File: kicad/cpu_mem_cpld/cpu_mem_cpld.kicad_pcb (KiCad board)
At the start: 4 copper layers, 160 x 100.3 mm, 52 parts, among them J1 USB, P5 CONN_02X25, U1 W65C02S, U10 74HCT245, U11 16550, U13 MAX232, U2 CHUCK, U3 28C256, U4 512k x 8, U5 74LS06, U6 NE555, U9 74HCT245, X1 OSC, X2 OSC

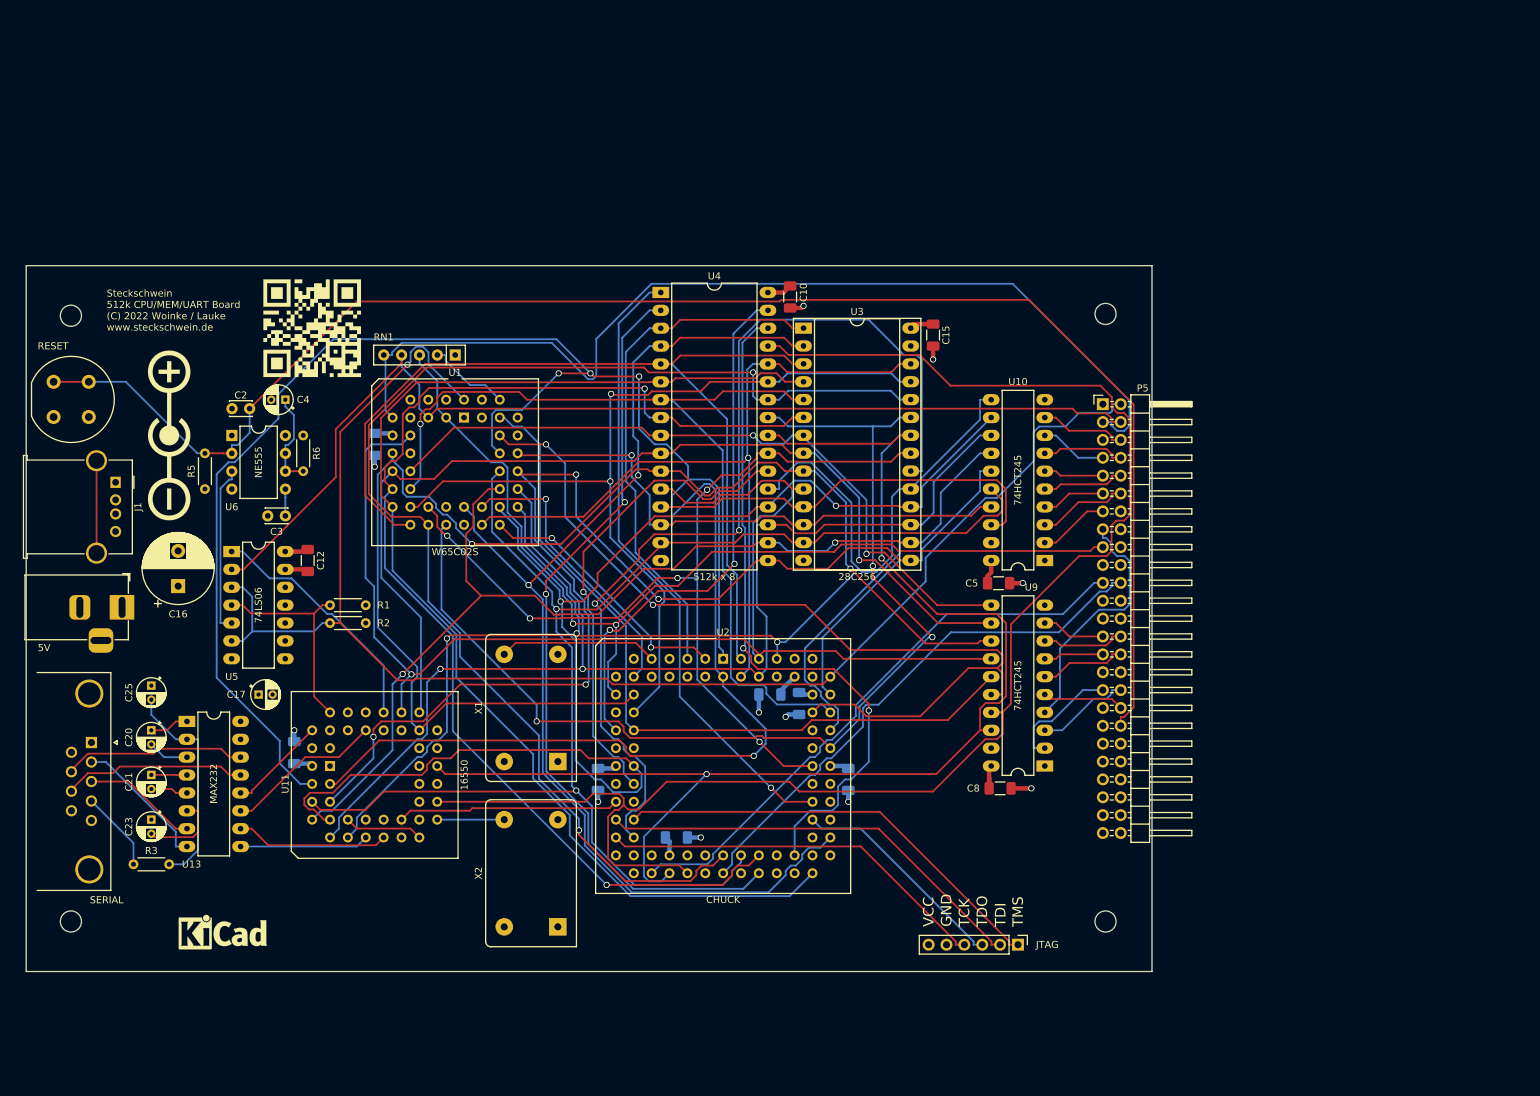
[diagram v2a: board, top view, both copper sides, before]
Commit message: added cs_uart2, /WE for EEPROM
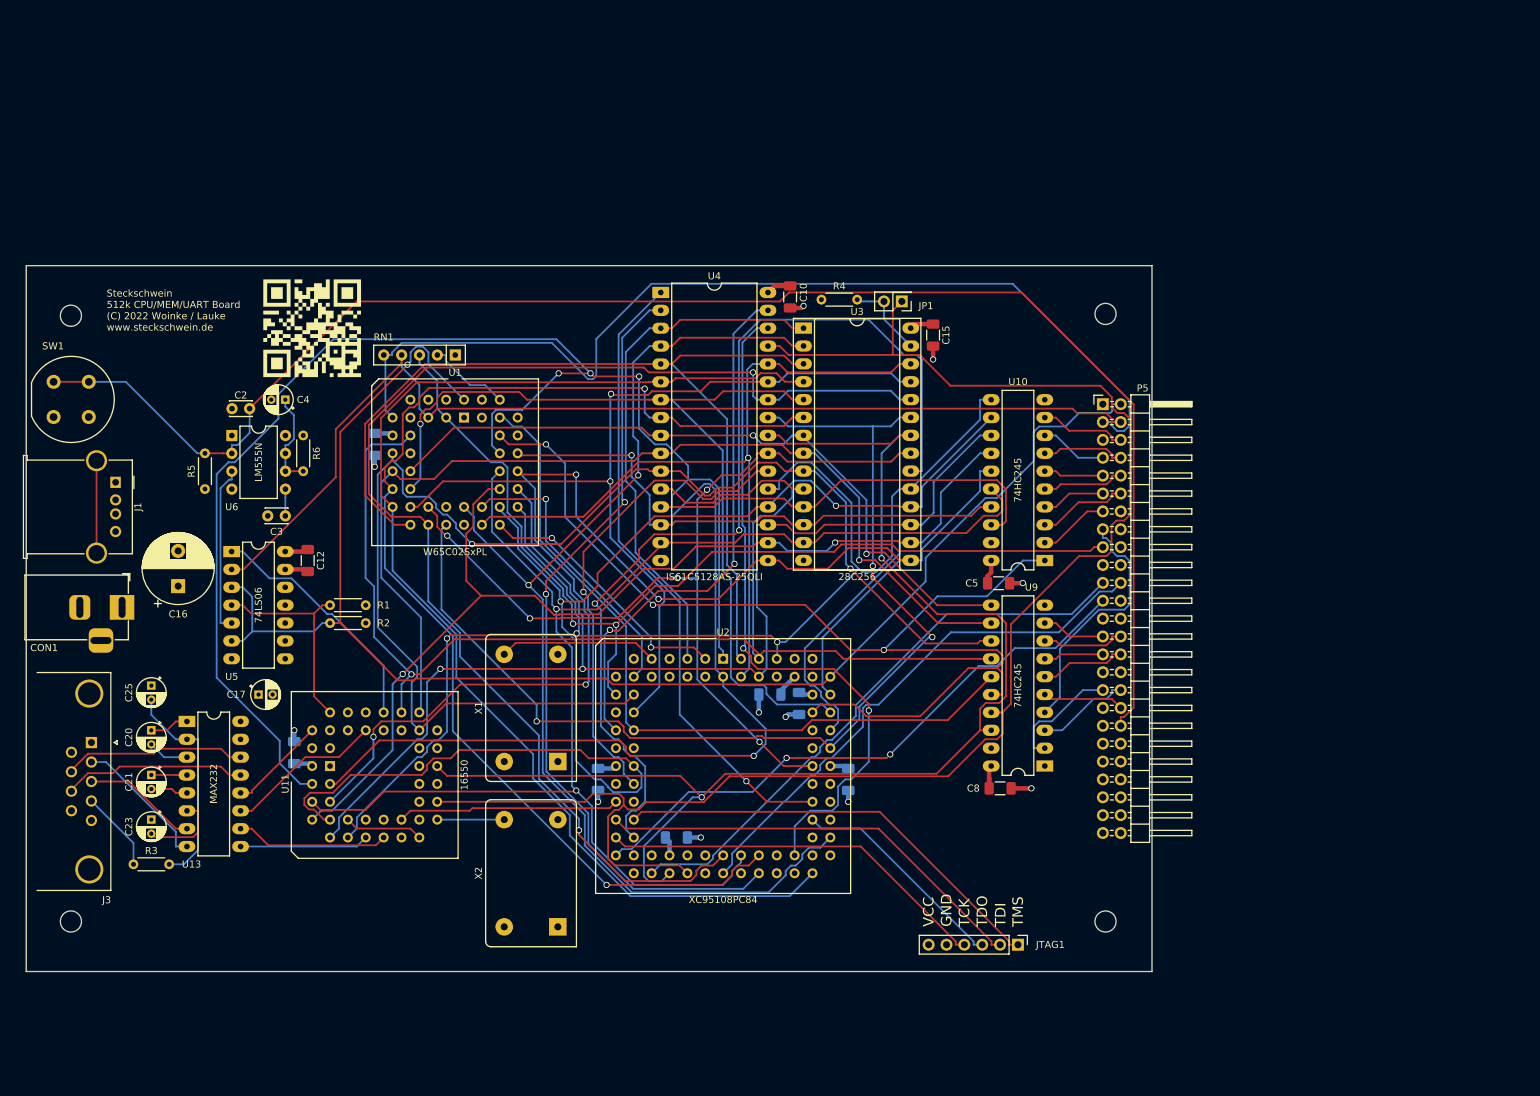
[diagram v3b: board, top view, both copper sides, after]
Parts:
- removed REF**: KiCad-Logo_5mm_SilkScreen, Symbol:KiCad-Logo_5mm_SilkScreen
- removed REF**: Polarity_Center_Positive_6mm_SilkScreen, Symbol:Polarity_Center_Positive_6mm_SilkScreen
- added JP1: Jumper_2_Open, Connector_PinHeader_2.54mm:PinHeader_2x01_P2.54mm_Vertical, F.Cu at (186.7, 50.8)
- added R4: 4k7, Resistor_THT:R_Axial_DIN0204_L3.6mm_D1.6mm_P5.08mm_Horizontal, F.Cu at (175.3, 50.5)
- U1: value W65C02S -> W65C02SxPL
- U10, U9: value 74HCT245 -> 74HC245
- U2: value CHUCK -> XC95108PC84
- U4: value 512k x 8 -> IS61C5128AS-25QLI
- U6: value NE555 -> LM555N
- renumbered 5V to CON1, SERIAL to J3, JTAG to JTAG1, RESET to SW1
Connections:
- U10 pad 1: /CPU_RW -> /CPU_R~{W}
- U2 pad 32: unconnected-(U2-Pad32) -> /~{CS_UART2}
- U3 pad 27: VCC -> Net-(U3-Pad27)
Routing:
- net /~{CS_UART2}: track 0.00 -> 84.2 mm, vias 0 -> 2
- net /CPU_R~{W}: track 126.9 -> 155.0 mm, vias 2 -> 3
- net Net-(U3-Pad27): track 0.00 -> 11.8 mm
- net /~{WE}: track 222.4 -> 229.4 mm
- net /RESET_TRIG: track 222.4 -> 223.2 mm
- net /EXT_A18: track 89.5 -> 90.1 mm

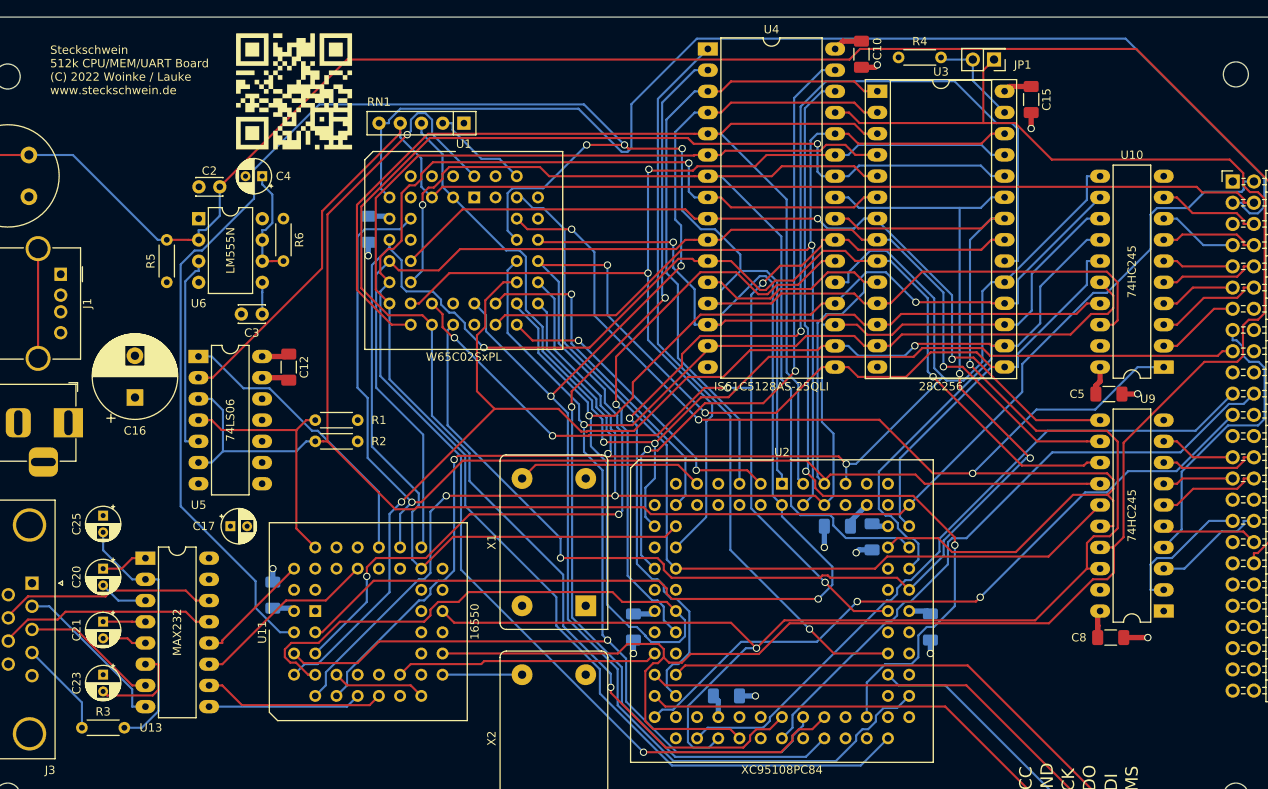
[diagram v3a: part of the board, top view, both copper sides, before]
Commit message: extra capacitor, revision text
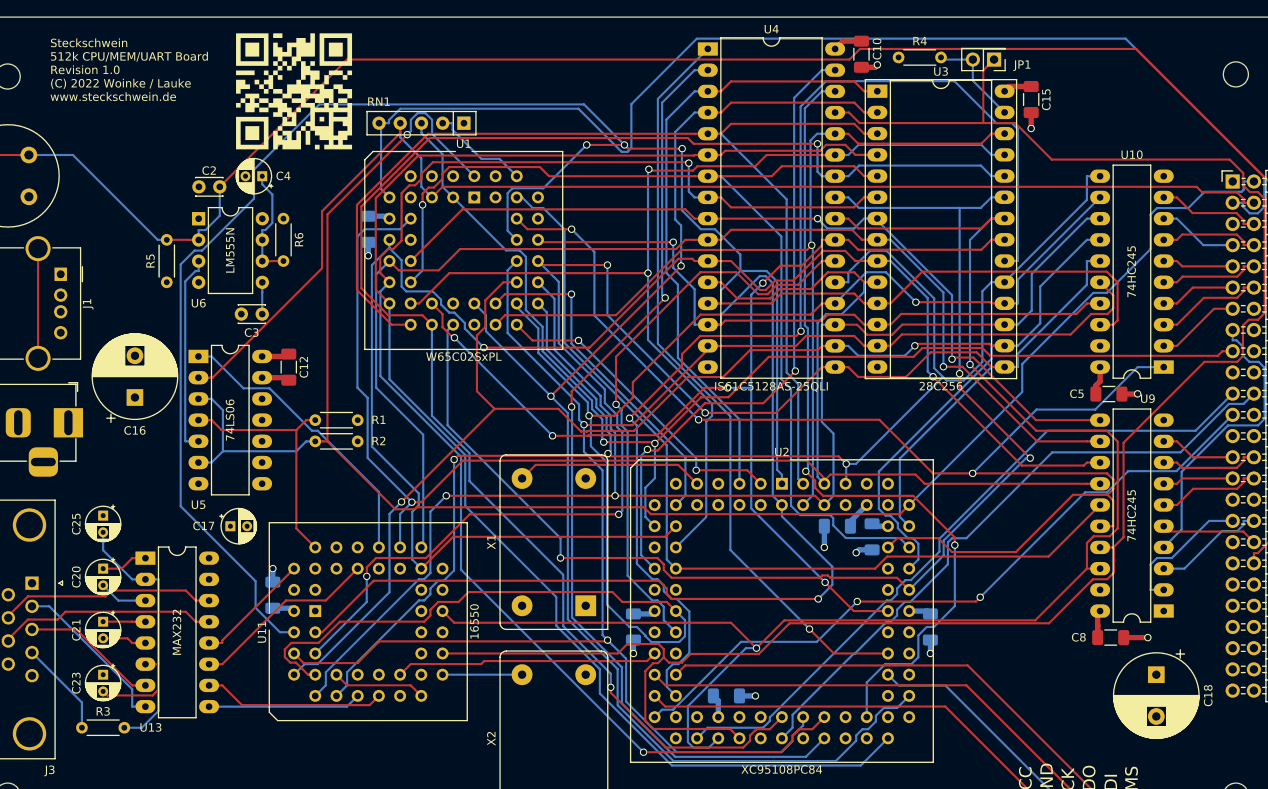
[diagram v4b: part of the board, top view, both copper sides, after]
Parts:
- added C18: 470µF, Capacitor_THT:CP_Radial_D10.0mm_P5.00mm, F.Cu at (206.1, 124.5)
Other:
- board text added: "Steckschwein 512k CPU/MEM/UART Board Revision 1.0 (C) 2022 Woinke / Lauke www.steckschwein.de"
- board text removed: "Steckschwein 512k CPU/MEM/UART Board (C) 2022 Woinke / Lauke www.steckschwein.de"
